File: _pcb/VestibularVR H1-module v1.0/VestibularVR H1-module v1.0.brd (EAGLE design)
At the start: 80 x 60 mm, 52 parts, among them IC1 FT232RL, IC2 74LVC1G07DBV, IC4 74LVC1G07DBV, IC5 74LVC1G07DBV, IC6 74LVC1G07DBV

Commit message: pcb v1.0 developed
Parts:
- removed C1: (no value), rcl:C0402
- removed F?, U$4: NDS332P, VestibularVR H1-module v1.0:SOT23
- removed JP1: Lick_port_1, pinhead:1X03
- removed JP10, JP9: Optical_flow_2, pinhead:1X05
- removed JP2: Lick_port_2, pinhead:1X03
- removed JP3: reward_valve_1, pinhead:1X03
- removed JP4: reward_valve_2, pinhead:1X03
- removed JP5: Camera_trigger_1, pinhead:1X02
- removed JP6: Camera_trigger_2, pinhead:1X02
- removed JP7: Optical_flow_1, pinhead:1X07
- removed JP8: Optical_flow_2, pinhead:1X07
- removed R4: (no value), rcl:R0402
- removed U$3: USBLC6-2SC6, VestibularVR H1-module v1.0:SOT23-6L
- added IC9: USBLC6-2SC6, VestibularVR H1-module v1.0:SOT23-6L
- added J1: reward_valve_1, SparkFun-Connectors:JST-3-PTH-VERT
- added J2: reward_valve_2, SparkFun-Connectors:JST-3-PTH-VERT
- added J3: lick_port_1, SparkFun-Connectors:JST-3-PTH-VERT
- added J4: lick_port_2, SparkFun-Connectors:JST-3-PTH-VERT
- added J5: Optical_flow_1, SparkFun-Connectors:2X4
- added J6: Optical_flow_2, SparkFun-Connectors:2X4
- added J7: Camera_trigger_1, SparkFun-Connectors:MOLEX-1X2
- added J8: Camera_trigger_2, SparkFun-Connectors:MOLEX-1X2
- moved R6 174.8 mm to (16.3, 50.9), turned to 180 degrees
- moved R5 173.1 mm to (16.3, 52.7), turned to 180 degrees
- moved R2 157.7 mm to (17.1, 43.9), turned to 180 degrees
- moved R3 154.8 mm to (51.0, 43.1), turned to 90 degrees
- moved C4 140.6 mm to (35.6, 54.4), turned to 90 degrees
- moved C6 138.5 mm to (34.3, 54.4), turned to 90 degrees
- moved R18 136.3 mm to (31.5, 54.3), turned to 270 degrees
- moved C5 134.1 mm to (30.1, 54.4), turned to 90 degrees
- moved C7 133.0 mm to (32.9, 54.4), turned to 90 degrees
- moved L1 127.6 mm to (44.1, 47.8)
- moved C2 123.2 mm to (48.9, 43.0), turned to 270 degrees
- moved C8 118.9 mm to (40.1, 46.4), turned to 90 degrees
- moved C3 116.4 mm to (45.3, 44.3), turned to 270 degrees
- moved C9 116.4 mm to (30.4, 39.6), turned to 270 degrees
- moved F1 73.6 mm to (45.8, 34.8), turned to 90 degrees
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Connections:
- removed net N$10: IC8.43
- removed net N$11: IC8.42
- removed net N$12: IC8.41
- removed net N$13: IC8.40
- removed net N$7: IC8.2
- removed net N$8: IC8.1
- new net LICK_PORT_1: IC6.2, J3.2
- new net LICK_PORT_2: IC5.2, J4.2
- new net U_LICK_PORT_1: IC6.4, IC8.40
- new net U_LICK_PORT_2: IC5.4, IC8.41
- new net U_REWARD_VALVE_1: IC8.2, U$6.1
- new net U_REWARD_VALVE_2: IC8.3, U$5.1
- net +3V3: now also J3.3, J4.3, J5.1, J6.1
- net +5V: now also D1.C, D2.C, J1.3, J2.3
- net GND: now also IC5.3, IC6.3, IC9.P$2, J3.1, J4.1, J5.7, J6.7, J7.1, J8.1, U$5.2, U$6.2; no longer JP5.2, JP6.2, U$3.P$2
- net N$16: now also IC2.4, J7.2; no longer IC2.2, JP5.1
- net N$2: now also IC9.P$6; no longer U$3.P$6
- net N$3: now also IC9.P$4; no longer U$3.P$4
- net N$4: now also IC4.4, J8.2; no longer IC4.2, JP6.1
- net N$6: now also D1.A, J2.1, U$5.3; no longer IC8.3
- net N$9: now also D2.A, J1.1, U$6.3; no longer IC8.44
- net USBDM: now also IC9.P$3; no longer U$3.P$3
- net USBDP: now also IC9.P$1; no longer U$3.P$1
- net USB_POWER: now also IC9.P$5; no longer U$3.P$5
- net U_CAM1_TRIGGER: now also IC2.2
- net U_CAM2_TRIGGER: now also IC4.2
- net U_OPTICAL_FLOW_1_CS: now also J5.2
- net U_OPTICAL_FLOW_1_INT: now also J5.5
- net U_OPTICAL_FLOW_1_MISO: now also J5.8
- net U_OPTICAL_FLOW_1_MOSI: now also J5.6
- net U_OPTICAL_FLOW_1_SCK: now also J5.4
- net U_OPTICAL_FLOW_2_CS: now also J6.2
- net U_OPTICAL_FLOW_2_INT: now also J6.5
- net U_OPTICAL_FLOW_2_MISO: now also J6.8
- net U_OPTICAL_FLOW_2_MOSI: now also J6.6
- net U_OPTICAL_FLOW_2_SCK: now also J6.4
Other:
- board size 80 x 60 mm -> 57.1 x 58.2 mm
- board text added: "Optical_flow_1"
- board text added: "Optical_flow_2"
- board text added: "camm_trigg_1"
- board text added: "camm_trigg_2"
- board text added: "lick_port_1"
- board text added: "lick_port_2"
- board text added: "reward_valve_1"
- board text added: "reward_valve_2"

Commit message: proceeding design VestibularVR H1
- Eagle version changed back to v.8.3.1
- proceeding design VestibularVR H1-module v1.0
- added Lick Sensor module v1.0
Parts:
- removed D2: BZX84CSMD, diode:TO236
- removed IC9: USBLC6-2SC6, VestibularVR H1-module v1.0:SOT23-6L
- removed J1: reward_valve_1, SparkFun-Connectors:JST-3-PTH-VERT
- removed J2: reward_valve_2, SparkFun-Connectors:JST-3-PTH-VERT
- removed J3: lick_port_1, SparkFun-Connectors:JST-3-PTH-VERT
- removed J4: lick_port_2, SparkFun-Connectors:JST-3-PTH-VERT
- removed J7: Camera_trigger_1, SparkFun-Connectors:MOLEX-1X2
- removed J8: Camera_trigger_2, SparkFun-Connectors:MOLEX-1X2
- removed OSC1: OSCILLATOR, harp camera controller:OSCILLATOR_3.2X2.5
- added C10, C11: 4.7uF, rcl:C0603
- added C12: 100nF, rcl:C0402
- added CAMERA_TRIGGER_1, CAMERA_TRIGGER_2, REWARD_VALVE_1, REWARD_VALVE_2: 22-23-2021, con-molex:22-23-2021
- added D4: BAT54, diode:SOT23
- added IC3: TLV70033DDCR, VestibularVR H1-module v1.0:TSOT23-5
- added IC7: USBLC6-2SC6, VestibularVR H1-module v1.0:SOT23-6L
- added LICK_PORT_1, LICK_PORT_2: 22-23-2031, con-molex:22-23-2031
- added R4, R7: 10k, rcl:R0402
- added U$2: OSCILLATOR, VestibularVR H1-module v1.0:OSCILLATOR_3.2X2.5
- added X7: 22-23-2051, con-molex:22-23-2051
- C8: device rcl:A/3216-18W -> rcl:A/3216-18R
- D1: value BZX84CSMD -> BAT54; device diode:TO236 -> diode:SOT23
- F1: device harp camera controller:R0603 -> VestibularVR H1-module v1.0:R0603
- IC8: value (none) -> ATXMEGA32A4U
- SV2: value (none) -> PINHD-2X3; device con-lstb:MA03-2 -> Connector:2X03
- moved R34 8.64 mm to (34.1, 34.4), turned to 90 degrees
- moved C8 6.62 mm to (34.5, 42.9)
- moved C4 6.31 mm to (34.7, 48.1), turned to 270 degrees
- moved C25 6.16 mm to (31.0, 36.0), turned to 180 degrees
- moved C27 5.61 mm to (27.7, 32.0)
- moved C9 5.52 mm to (25.0, 38.5)
- moved C3 5.43 mm to (39.9, 43.5), turned to 180 degrees
- moved L1 4.91 mm to (39.6, 46.0)
- moved R1 4.82 mm to (15.5, 41.6)
- moved R5 4.13 mm to (15.5, 48.7)
- moved IC6 3.87 mm to (10.9, 23.5)
- moved J5 3.83 mm to (41.7, 6.02)
- moved IC8 3.59 mm to (29.9, 22.6)
- moved C26 3.59 mm to (39.5, 24.8)
- moved U$5 3.57 mm to (11.1, 8.59)
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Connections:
- removed net N$15: C5.1, C8.+, IC1.20, L1.1
- removed net U_HARP_H1_BOARD_RX: IC8.22
- removed net U_HARP_H1_BOARD_TX: IC8.23
- removed net VDD: C25.1, C26.1, C27.1, C28.1, C29.1, C30.1, F1.1, IC8.19, IC8.31, IC8.39, IC8.9, OSC1.P$4, R34.2, SV2.6
- new net +12V: X7.5
- new net +3V3_U: C25.1, C26.1, C27.1, C28.1, C29.1, C30.1, F1.1, IC8.19, IC8.31, IC8.39, IC8.9, R34.2, SV2.6, U$2.P$4
- new net HARP_H1_BOARD_RX: IC8.22, X7.3
- new net HARP_H1_BOARD_TX: IC8.23, X7.4
- new net HARP_H1_CLOCK_IN: IC8.12, X7.2
- new net N$7: D4.3, REWARD_VALVE_2.2
- new net N$8: D1.3, REWARD_VALVE_1.2
- net +3V3: now also C11.1, C12.1, IC3.5, IC5.5, IC6.5, LICK_PORT_1.3, LICK_PORT_2.3; no longer J3.3, J4.3
- net +5V: now also C10.1, C5.1, C8.+, IC1.20, IC3.1, IC3.3, L1.1; no longer D1.C, D2.C, J1.3, J2.3
- net GND: now also C10.2, C11.2, C12.2, CAMERA_TRIGGER_1.1, CAMERA_TRIGGER_2.1, IC3.2, IC7.P$2, LICK_PORT_1.1, LICK_PORT_2.1, R4.1, R7.1, U$2.P$2, X7.1; no longer IC9.P$2, J3.1, J4.1, J7.1, J8.1, OSC1.P$2
- net LICK_PORT_1: now also LICK_PORT_1.2; no longer J3.2
- net LICK_PORT_2: now also LICK_PORT_2.2; no longer J4.2
- net N$16: now also CAMERA_TRIGGER_1.2; no longer J7.2
- net N$2: now also IC7.P$4; no longer IC9.P$6
- net N$3: now also IC7.P$6; no longer IC9.P$4
- net N$4: now also CAMERA_TRIGGER_2.2; no longer J8.2
- net N$6: now also D4.1, REWARD_VALVE_2.1; no longer D1.A, J2.1
- net N$9: now also D1.1, REWARD_VALVE_1.1; no longer D2.A, J1.1
- net OSC2: now also U$2.P$3; no longer OSC1.P$3
- net USBDM: now also IC7.P$1; no longer IC9.P$3
- net USBDP: now also IC7.P$3; no longer IC9.P$1
- net USB_POWER: now also IC7.P$5; no longer IC9.P$5
- net U_CAM2_TRIGGER: now also IC8.20; no longer IC8.5
- net U_OPTICAL_FLOW_1_INT: no longer IC8.20
- net U_OPTICAL_FLOW_2_INT: no longer IC8.21
- net U_REWARD_VALVE_1: now also R4.2
- net U_REWARD_VALVE_2: now also R7.2
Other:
- board size 57.1 x 58.2 mm -> 56 x 57 mm

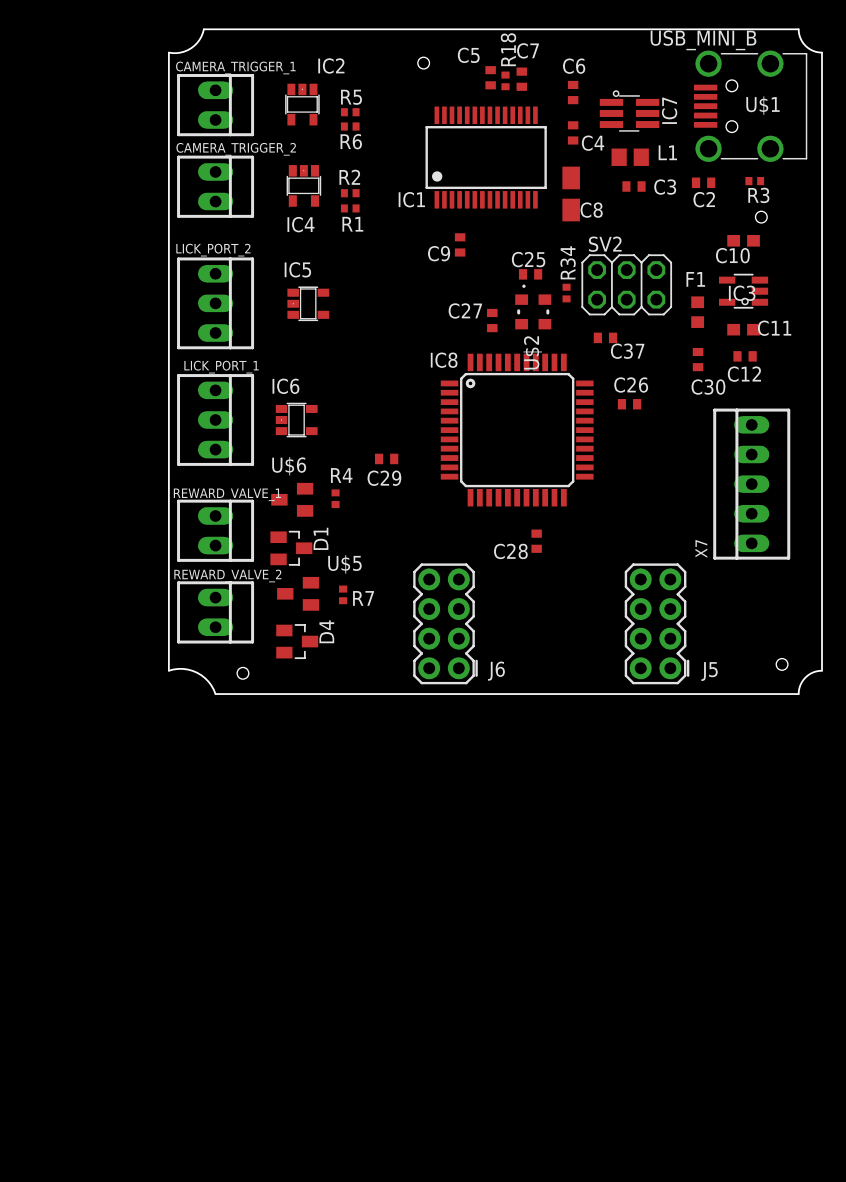
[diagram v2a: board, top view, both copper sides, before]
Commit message: update on VestibularVR & LickSensor
- returned to Eagle 9.6.2
- projects reviewed with Filipe
- LickSensor board with reviews already made
- VestibularVR  board starting implementing reviews
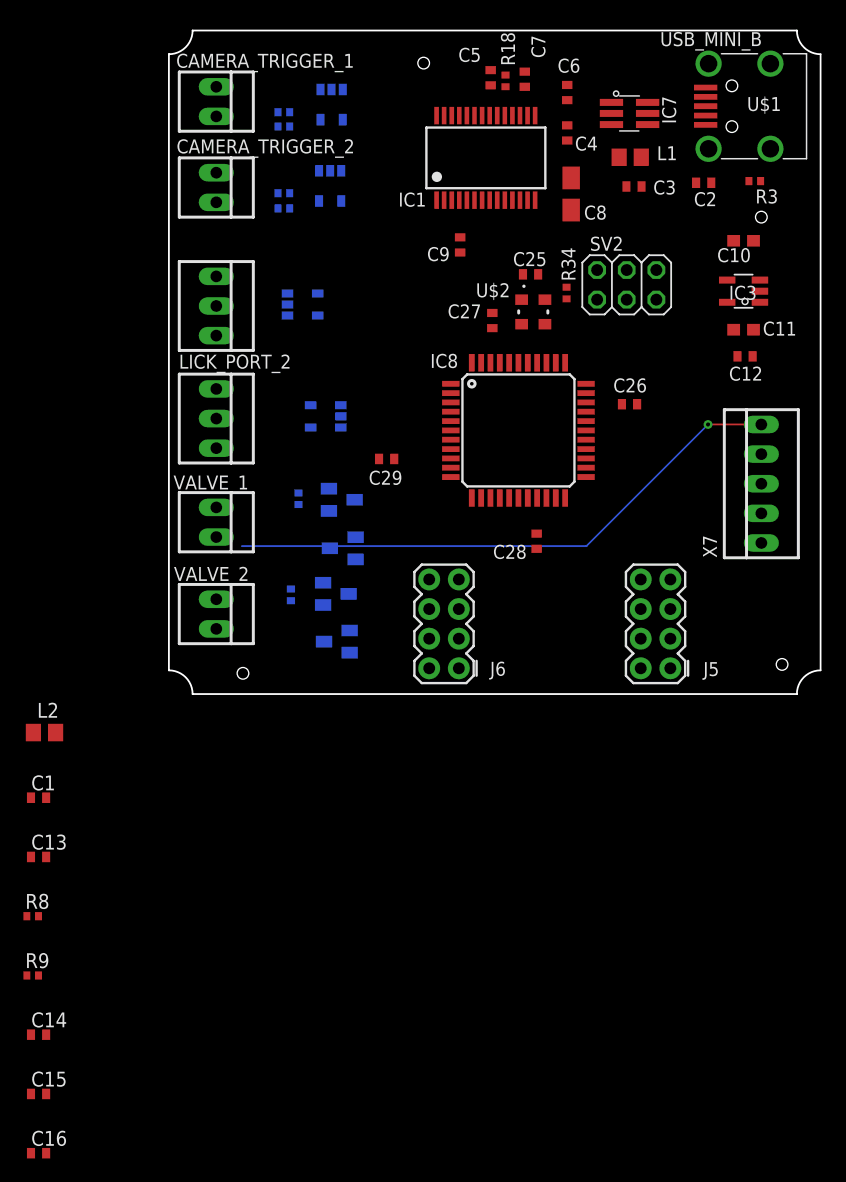
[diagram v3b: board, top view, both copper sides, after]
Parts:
- removed C30, C37: 330pF, rcl:C0402
- removed F1: 330 Ohms @ 100MHz, VestibularVR H1-module v1.0:R0603
- removed REWARD_VALVE_1, REWARD_VALVE_2: 22-23-2021, con-molex:22-23-2021
- added C1, C14, C15, C16: 100nF, rcl:C0402
- added C13: 47pF, rcl:C0402
- added L2: 40R@100MHz, rcl:R0805
- added R8, R9: 10k, rcl:R0402
- added VALVE_1, VALVE_2: 22-23-2021, con-molex:22-23-2021
- moved IC6 9.92 mm to (11.5, 33.4), flipped to the bottom, turned to 90 degrees
- moved LICK_PORT_2 9.88 mm to (4.06, 23.6)
- moved LICK_PORT_1 9.77 mm to (4.06, 33.3)
- moved IC5 9.77 mm to (13.5, 23.8), flipped to the bottom
- moved R1 5.70 mm to (9.85, 41.6), flipped to the bottom
- moved R2 5.70 mm to (9.85, 42.9), flipped to the bottom
- moved R5 5.70 mm to (9.85, 48.7), flipped to the bottom
- moved R6 5.70 mm to (9.85, 49.9), flipped to the bottom
- moved R7 4.47 mm to (10.5, 8.50), flipped to the bottom
- moved D1 4.40 mm to (14.9, 12.5), flipped to the bottom
- moved U$6 4.24 mm to (14.8, 16.7), flipped to the bottom
- moved D4 3.40 mm to (14.4, 4.50), flipped to the bottom
- moved U$5 3.24 mm to (14.3, 8.59), flipped to the bottom
- moved R4 3.18 mm to (11.1, 16.7), flipped to the bottom
- moved IC2 2.50 mm to (14.0, 50.6), flipped to the bottom
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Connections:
- removed net N$8: D1.3, REWARD_VALVE_1.2
- removed net U_HARPH1CLOCKIN: IC8.7
- net +12V: now also D1.3, VALVE_1.2
- net +3V3: now also L2.2; no longer F1.2
- net +3V3_U: now also C1.1, L2.1; no longer C30.1, F1.1
- net GND: now also C1.2, C13.2, R8.1, R9.1; no longer C30.2, C37.2
- net LICK_PORT_1: now also R9.2
- net LICK_PORT_2: now also R8.2
- net N$6: now also VALVE_2.1; no longer REWARD_VALVE_2.1
- net N$7: now also VALVE_2.2; no longer REWARD_VALVE_2.2
- net N$9: now also VALVE_1.1; no longer REWARD_VALVE_1.1
- net PDI_CLK: now also C13.1; no longer C37.1
- net U_CAM1_TRIGGER: now also IC8.10; no longer IC8.4
- net U_OPTICAL_FLOW_1_INT: now also IC8.4
- net U_OPTICAL_FLOW_2_CS: no longer IC8.14
- net U_OPTICAL_FLOW_2_INT: now also IC8.5
- net U_OPTICAL_FLOW_2_MISO: no longer IC8.16
- net U_OPTICAL_FLOW_2_MOSI: no longer IC8.15
- net U_OPTICAL_FLOW_2_SCK: no longer IC8.17
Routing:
- net +12V: track 0.00 -> 48.9 mm, vias 0 -> 1
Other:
- board size 56 x 57 mm -> 55.9 x 56.9 mm

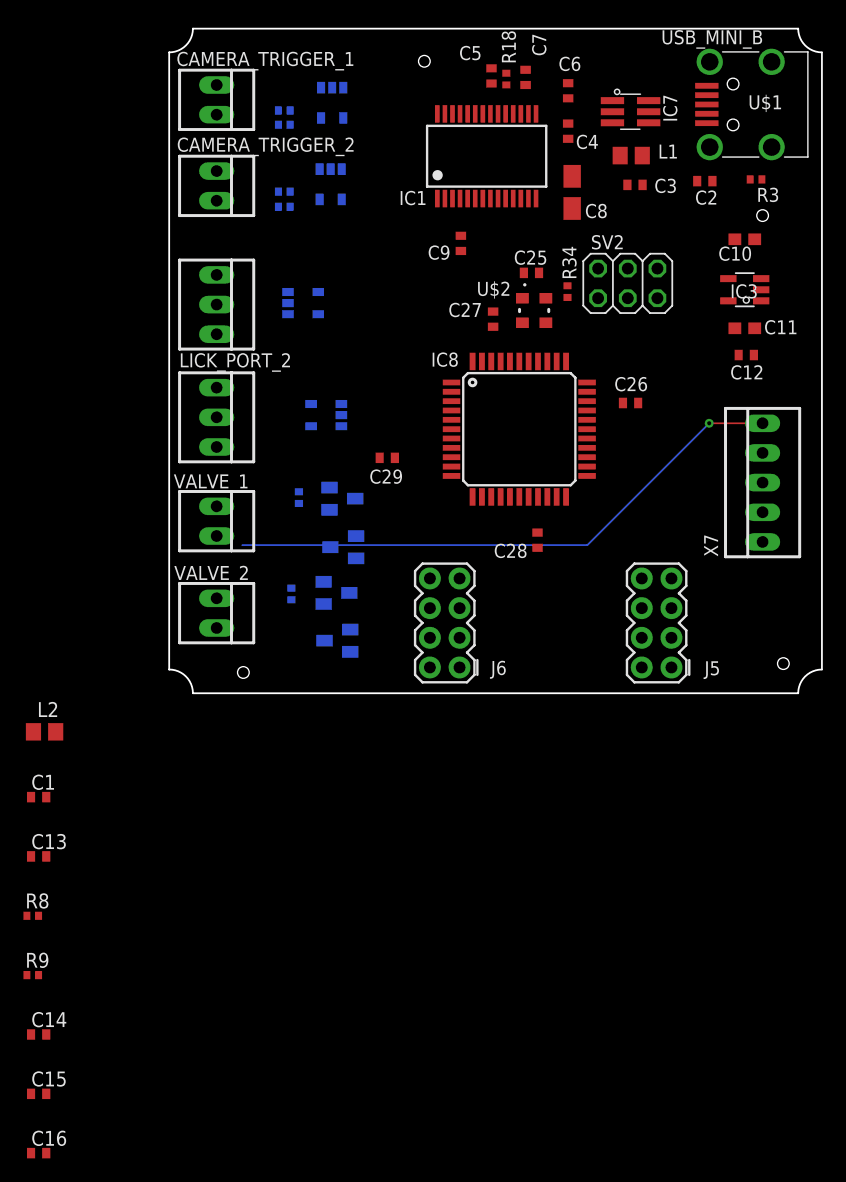
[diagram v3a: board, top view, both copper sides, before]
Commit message: VestibularVR H1-module v1.0 - revisions made with Filipe updated
Revisions made:
- added missing decoupler caps
- considered components on top & bottom side
- review pinout on micro

Next steps:
- final mechanical integration
- final plugs choose
.. and.. something more??
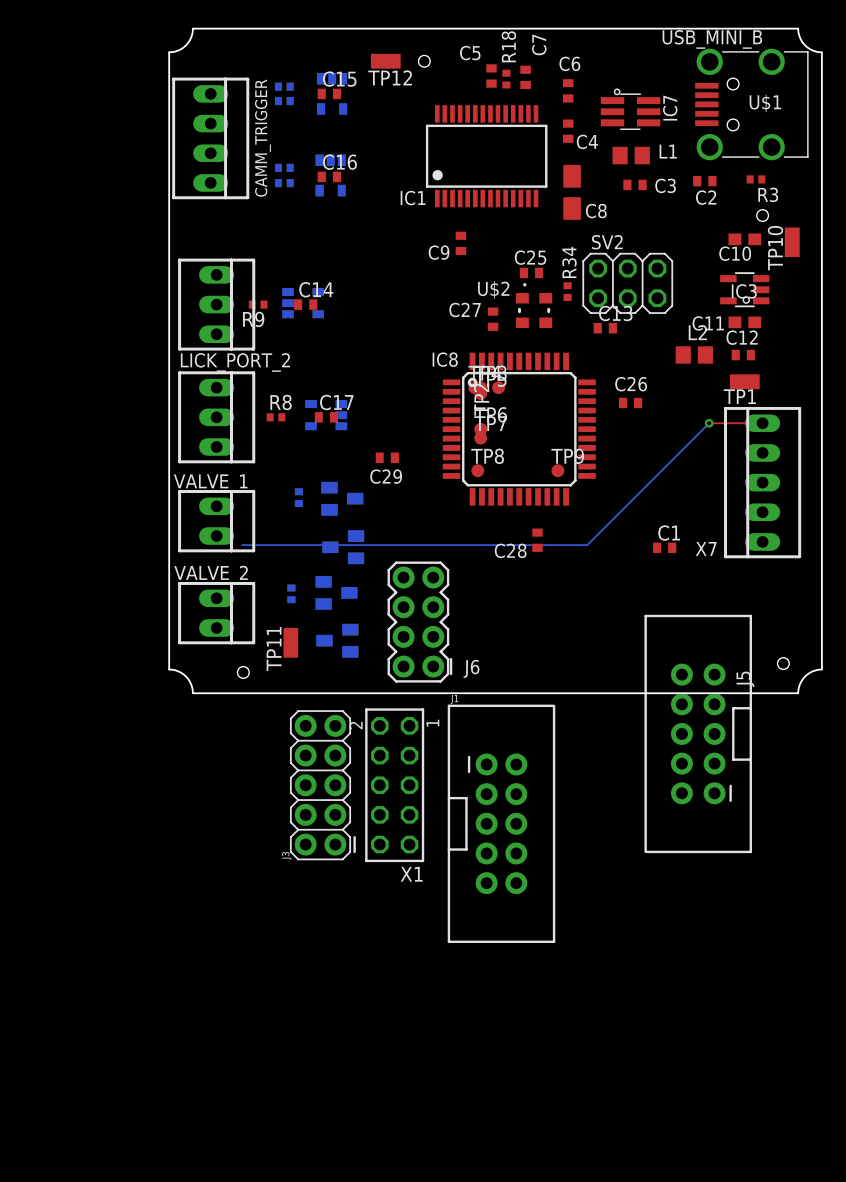
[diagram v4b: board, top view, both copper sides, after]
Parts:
- removed CAMERA_TRIGGER_1, CAMERA_TRIGGER_2: 22-23-2021, con-molex:22-23-2021
- added C17: 100nF, rcl:C0402
- added CAMM_TRIGGER: 22-23-2041, con-molex:22-23-2041
- added J1: (no value), SparkFun-Connectors:2X5-SHROUDED
- added J3: (no value), SparkFun-Connectors:2X5
- added TP1, TP10, TP11, TP12: WIREPADSMD1,27-254, wirepad:SMD1,27-2,54
- added TP2, TP3, TP4, TP5, TP6, TP7, TP8, TP9: WIREPADSMD1,27-254, testpad:TP11R
- added X1: TSW-105-02-S-D, con-samtec:TSW-105-02-S-D
- J5: device SparkFun-Connectors:2X4 -> SparkFun-Connectors:2X5-SHROUDED_LOCK
- moved C15 89.1 mm to (13.7, 51.3)
- moved C16 87.2 mm to (13.7, 44.2)
- moved C14 66.5 mm to (11.7, 33.3)
- moved C13 66.3 mm to (37.3, 31.2)
- moved L2 64.3 mm to (45.0, 29.0)
- moved R9 60.6 mm to (7.62, 33.3), turned to 180 degrees
- moved C1 57.7 mm to (42.4, 12.4)
- moved R8 47.5 mm to (9.14, 23.6)
- moved J5 10.1 mm to (45.3, -3.48), turned to 180 degrees
- moved J6 2.26 mm to (21.3, 6.10)
- moved R5 2.03 mm to (9.85, 50.7)
- moved R6 2.03 mm to (9.85, 51.9)
- moved R1 2.03 mm to (9.85, 43.7)
- moved R2 2.03 mm to (9.85, 45.0)
- moved IC2 0.76 mm to (14.0, 51.3)
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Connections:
- new net N$10: IC8.43, TP3.TP
- new net N$11: IC8.44, TP4.TP
- new net N$12: IC8.1, TP5.TP
- new net N$13: IC8.6, TP6.TP
- new net N$15: IC8.7, TP7.TP
- new net N$17: IC8.11, TP8.TP
- new net N$18: IC8.21, TP9.TP
- new net N$8: IC8.42, TP2.TP
- net +3V3: now also C14.1, C17.1, TP1.1
- net +5V: now also TP10.1
- net GND: now also C14.2, C15.2, C16.2, C17.2, CAMM_TRIGGER.1, CAMM_TRIGGER.3, TP11.1, TP12.1; no longer CAMERA_TRIGGER_1.1, CAMERA_TRIGGER_2.1
- net N$14: now also C15.1
- net N$16: now also CAMM_TRIGGER.4; no longer CAMERA_TRIGGER_1.2
- net N$4: now also CAMM_TRIGGER.2; no longer CAMERA_TRIGGER_2.2
- net N$5: now also C16.1
- net U_OPTICAL_FLOW_1_CS: now also IC8.14; no longer IC8.24
- net U_OPTICAL_FLOW_1_MISO: now also IC8.16; no longer IC8.26
- net U_OPTICAL_FLOW_1_MOSI: now also IC8.15; no longer IC8.25
- net U_OPTICAL_FLOW_1_SCK: now also IC8.17; no longer IC8.27
- net U_OPTICAL_FLOW_2_CS: now also IC8.24
- net U_OPTICAL_FLOW_2_MISO: now also IC8.26
- net U_OPTICAL_FLOW_2_MOSI: now also IC8.25
- net U_OPTICAL_FLOW_2_SCK: now also IC8.27
